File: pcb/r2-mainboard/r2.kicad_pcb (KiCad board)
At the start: 2 copper layers, 185.5 x 95 mm, 22 parts, among them J21 MICRO_SD(TFC-WPAPR-08), J22 HC-FPC-05-09-6RLTAG, J23 HC-FPC-05-09-6RLTAG, J24 HC-FPC-05-09-8RLTAG, J25 SolderPads 3x, J26 BTH-060-01-L-D-A-K-TR, J27 BTH-060-01-L-D-A-K-TR, J6 FPC-05F-50PH20, U13 TPS63802DLAR, U41 XC6SLX-FTG256, U52 MT41K64M16TW, U53 LM3630A, X2 PCM-071

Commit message: R2: a script to repair KiCad's library paths, instead of instructions
The owner does not run the AppImage -- KiCad is an extracted AppDir at
~/Apps/kicad-10.0.4 (a symlink to ./AppDir) launched via AppRun. That makes
the diagnosis better, not worse: /tmp/.mount_<random> is where an AppImage
mounts itself while running, so the entry in fp-lib-table is a leftover
written during an AppImage run before the extraction, and dead ever since.
The symbol table never broke because it was written with absolute paths.

tools/fix_kicad_paths.sh replaces the hand instructions. It derives the
paths from the install rather than hardcoding them, verifies all 155
library paths exist BEFORE installing anything, backs up both files with a
timestamp, and refuses to run while KiCad is open -- KiCad rewrites these
on exit and would silently undo the fix. It also sets the three path
variables, which were literally "vars": null, and then probes four
footprints and the 3D model tree to prove the result rather than assert it.

Dry-run against a copy of the real config: 155 libraries installed and
verified, the three variables set, every other key in kicad_common.json
preserved, and the real config untouched.

Co-Authored-By: Claude Opus 5 <noreply@anthropic.com>
Claude-Session: https://claude.ai/code/session_01MnesETWABbVdbcVnCKfKVs
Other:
- copper layers 2 -> 4
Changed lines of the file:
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@@
 	(generator_version "10.0")
 	(general
-		(thickness 1.6)
+		(thickness 1.0044)
 		(legacy_teardrops no)
 	)
@@
 	(layers
 		(0 "F.Cu" signal)
+		(4 "In1.Cu" power)
+		(6 "In2.Cu" mixed)
 		(2 "B.Cu" signal)
 		(9 "F.Adhes" user "F.Adhesive")
@@
 	)
 	(setup
+		(stackup
+			(layer "F.SilkS"
+				(type "Top Silk Screen")
+				(color "White")
+			)
+			(layer "F.Paste"
+				(type "Top Solder Paste")
+			)
+			(layer "F.Mask"
+				(type "Top Solder Mask")
+				(color "Green")
+				(thickness 0.025)
+			)
+			(layer "F.Cu"
+				(type "copper")
+				(thickness 0.035)
+			)
+			(layer "dielectric 1"
+				(type "prepreg")
+				(thickness 0.127)
+				(material "FR4")
+				(epsilon_r 4.2)
+				(loss_tangent 0.02)
+			)
+			(layer "In1.Cu"
+				(type "copper")
+				(thickness 0.0152)
+			)
+			(layer "dielectric 2"
+				(type "core")
+				(thickness 0.6)
+				(material "FR4")
+				(epsilon_r 4.2)
+				(loss_tangent 0.02)
+			)
+			(layer "In2.Cu"
+				(type "copper")
+				(thickness 0.0152)
+			)
+			(layer "dielectric 3"
+				(type "prepreg")
+				(thickness 0.127)
+				(material "FR4")
+				(epsilon_r 4.2)
+				(loss_tangent 0.02)
+			)
+			(layer "B.Cu"
+				(type "copper")
+				(thickness 0.035)
+			)
+			(layer "B.Mask"
+				(type "Bottom Solder Mask")
+				(color "Green")
+				(thickness 0.025)
+			)
+			(layer "B.Paste"
+				(type "Bottom Solder Paste")
+			)
+			(layer "B.SilkS"
+				(type "Bottom Silk Screen")
+				(color "White")
+			)
+			(copper_finish "ENIG")
+			(dielectric_constraints no)
+		)
 		(pad_to_mask_clearance 0)
 		(allow_soldermask_bridges_in_footprints no)
@@
 		(capping no)
 		(filling no)
+		(zone_defaults)
 		(pcbplotparams
 			(layerselection 0x00000000_00000000_55555555_5755f5ff)
@@
 		)
 		(embedded_fonts no)
-		(model "${KICAD8_3DMODEL_DIR}/Diode_SMD.3dshapes/D_SOD-323.wrl"
+		(model "${KICAD10_3DMODEL_DIR}/Diode_SMD.3dshapes/D_SOD-323.step"
 			(offset
 				(xyz 0 0 0)
@@
 		)
 		(embedded_fonts no)
-		(model "${KICAD6_3DMODEL_DIR}/Package_BGA.3dshapes/BGA-96_9.0x13.0mm_Layout2x3x16_P0.8mm.wrl"
+		(model "${KICAD10_3DMODEL_DIR}/Package_BGA.3dshapes/BGA-96_9.0x13.0mm_Layout2x3x16_P0.8mm.step"
 			(offset
 				(xyz 0 0 0)
@@
 		)
 		(embedded_fonts no)
-		(model "${KICAD8_3DMODEL_DIR}/Diode_SMD.3dshapes/D_SOD-323.wrl"
+		(model "${KICAD10_3DMODEL_DIR}/Diode_SMD.3dshapes/D_SOD-323.step"
 			(offset
 				(xyz 0 0 0)
@@
 		)
 		(embedded_fonts no)
-		(model "${KICAD8_3DMODEL_DIR}/Connector_FFC-FPC.3dshapes/Hirose_FH12-8S-0.5SH_1x08-1MP_P0.50mm_Horizontal.wrl"
+		(model "${KICAD10_3DMODEL_DIR}/Connector_FFC-FPC.3dshapes/Hirose_FH12-8S-0.5SH_1x08-1MP_P0.50mm_Horizontal.step"
 			(offset
 				(xyz 0 0 0)
@@
 		)
 		(embedded_fonts no)
-		(model "${KICAD8_3DMODEL_DIR}/Diode_SMD.3dshapes/D_SOD-323.wrl"
+		(model "${KICAD10_3DMODEL_DIR}/Diode_SMD.3dshapes/D_SOD-323.step"
 			(offset
 				(xyz 0 0 0)
@@
 		)
 		(embedded_fonts no)
-		(model "${KICAD8_3DMODEL_DIR}/Diode_SMD.3dshapes/D_SOD-323.wrl"
+		(model "${KICAD10_3DMODEL_DIR}/Diode_SMD.3dshapes/D_SOD-323.step"
 			(offset
 				(xyz 0 0 0)
@@
 		)
 		(embedded_fonts no)
-		(model "${KICAD8_3DMODEL_DIR}/Connector_FFC-FPC.3dshapes/Hirose_FH12-8S-0.5SH_1x08-1MP_P0.50mm_Horizontal.wrl"
+		(model "${KICAD10_3DMODEL_DIR}/Connector_FFC-FPC.3dshapes/Hirose_FH12-8S-0.5SH_1x08-1MP_P0.50mm_Horizontal.step"
 			(offset
 				(xyz 0 0 0)
@@
 		)
 		(embedded_fonts no)
-		(model "${KICAD8_3DMODEL_DIR}/Diode_SMD.3dshapes/D_SOD-323.wrl"
+		(model "${KICAD10_3DMODEL_DIR}/Diode_SMD.3dshapes/D_SOD-323.step"
 			(offset
 				(xyz 0 0 0)
@@
 		)
 		(embedded_fonts no)
-		(model "${KICAD8_3DMODEL_DIR}/Diode_SMD.3dshapes/D_SOD-323.wrl"
+		(model "${KICAD10_3DMODEL_DIR}/Diode_SMD.3dshapes/D_SOD-323.step"
 			(offset
 				(xyz 0 0 0)
@@
 		)
 		(embedded_fonts no)
-		(model "${KICAD8_3DMODEL_DIR}/Diode_SMD.3dshapes/D_SOD-323.wrl"
+		(model "${KICAD10_3DMODEL_DIR}/Diode_SMD.3dshapes/D_SOD-323.step"
 			(offset
 				(xyz 0 0 0)
@@
 		)
 		(embedded_fonts no)
-		(model "${KICAD8_3DMODEL_DIR}/Diode_SMD.3dshapes/D_SOD-323.wrl"
+		(model "${KICAD10_3DMODEL_DIR}/Diode_SMD.3dshapes/D_SOD-323.step"
 			(offset
 				(xyz 0 0 0)
@@
 		)
 		(embedded_fonts no)
-		(model "${KICAD8_3DMODEL_DIR}/Diode_SMD.3dshapes/D_SOD-323.wrl"
+		(model "${KICAD10_3DMODEL_DIR}/Diode_SMD.3dshapes/D_SOD-323.step"
 			(offset
 				(xyz 0 0 0)

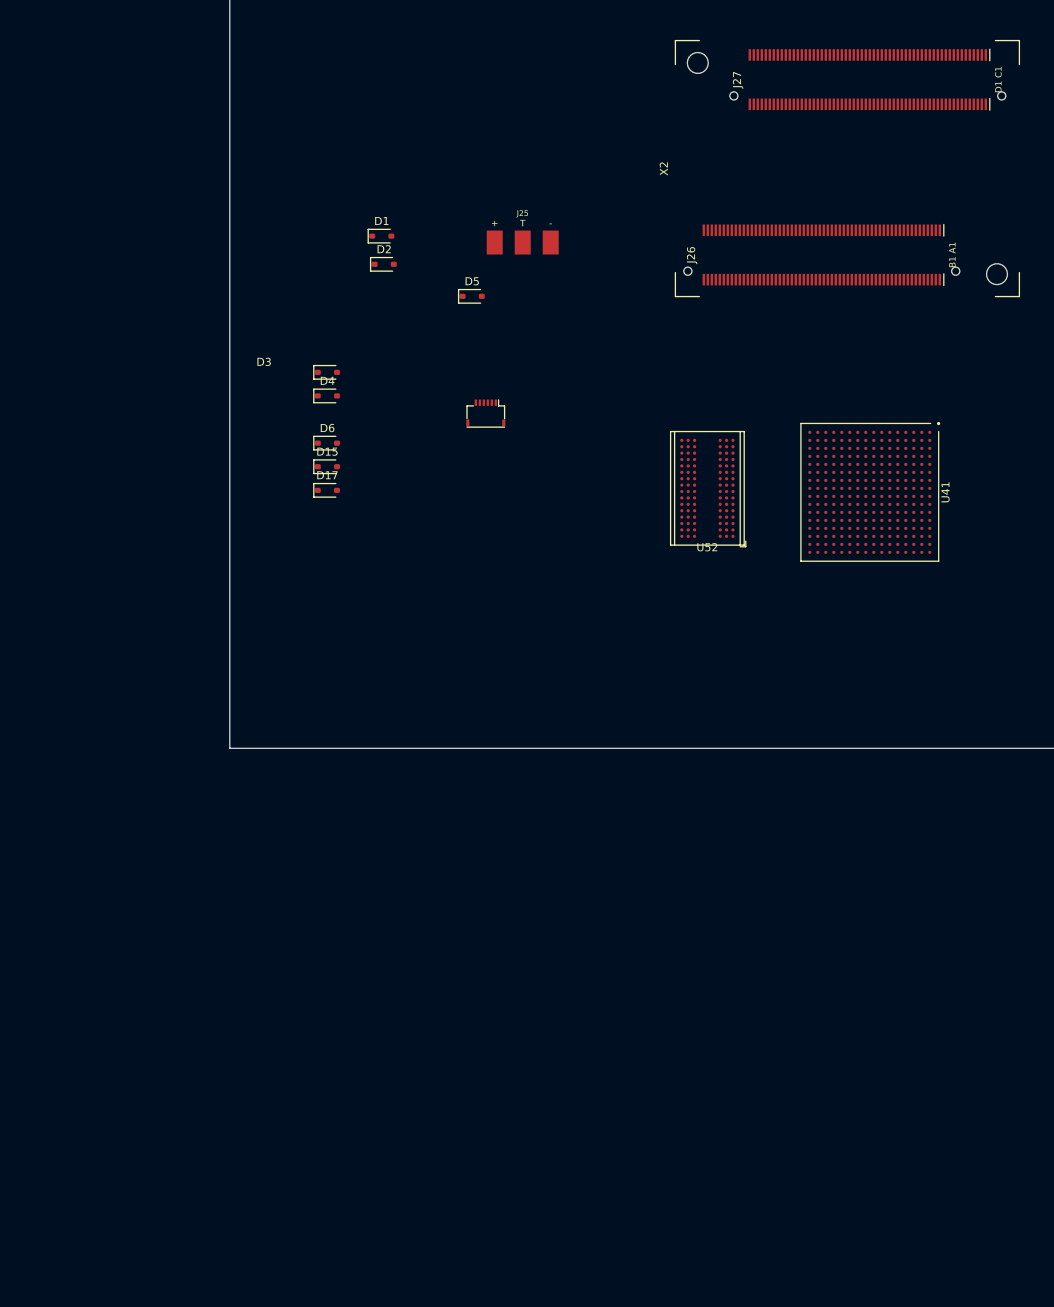
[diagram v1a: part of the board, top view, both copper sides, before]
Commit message: R2: place the two receptacles from X2, and fix three bugs found doing it
The connectors move as one now. tools/place_som.py reads X2's position and
rotation, snaps J26/J27 onto their exact offsets, and puts all three into a
KiCad group -- so from here you drag the SoM, not three parts that have to
agree with each other. It backs up the board, refuses to run while KiCad is
open, and re-runs the geometry check to prove its own result.

That symmetry is the reason this is a tool and not an instruction: the two
offsets are exact negatives about X2's origin, so an error of the wrong kind
does not shift a connector slightly, it puts J26 where J27 belongs. The
module still seats and every one of 240 nets is on the wrong receptacle.

Three bugs, all mine:

1. check_pcb_connectors.py had the rotation sign backwards, which SWAPPED
   the two expected positions. It reported a hand placement that was 0.9 mm
   and 0.2 mm out as 22 mm out, and would equally have blessed a board with
   the connectors exchanged. Settled empirically from a drill export rather
   than by reasoning: J26's alignment holes are asymmetric in x, so they
   distinguish the conventions. Confirmed twice, against X2's M2.5 holes too.

2. gen_som_footprint.py wrote (layer "User.Drawings"), which is KiCad's
   display alias; a board file needs the canonical Dwgs.User. The footprint
   editor accepts the alias, so the library exported fine -- but on import
   Pcbnew put those rects on a layer literally named "Rescue", and from then
   on kicad-cli could not read the board at all. Every pcb subcommand had
   been failing since the board was created.

3. Which made a third bug visible: check_pcb.py read /tmp/r2-drc.json
   without checking that the run succeeded, so it reported the previous
   run's numbers. A board that would not open was described as having 4250
   DRC violations. It now deletes the report first and says DID NOT RUN.

Real DRC, now that it runs: 742 violations, 499 unconnected -- which is what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
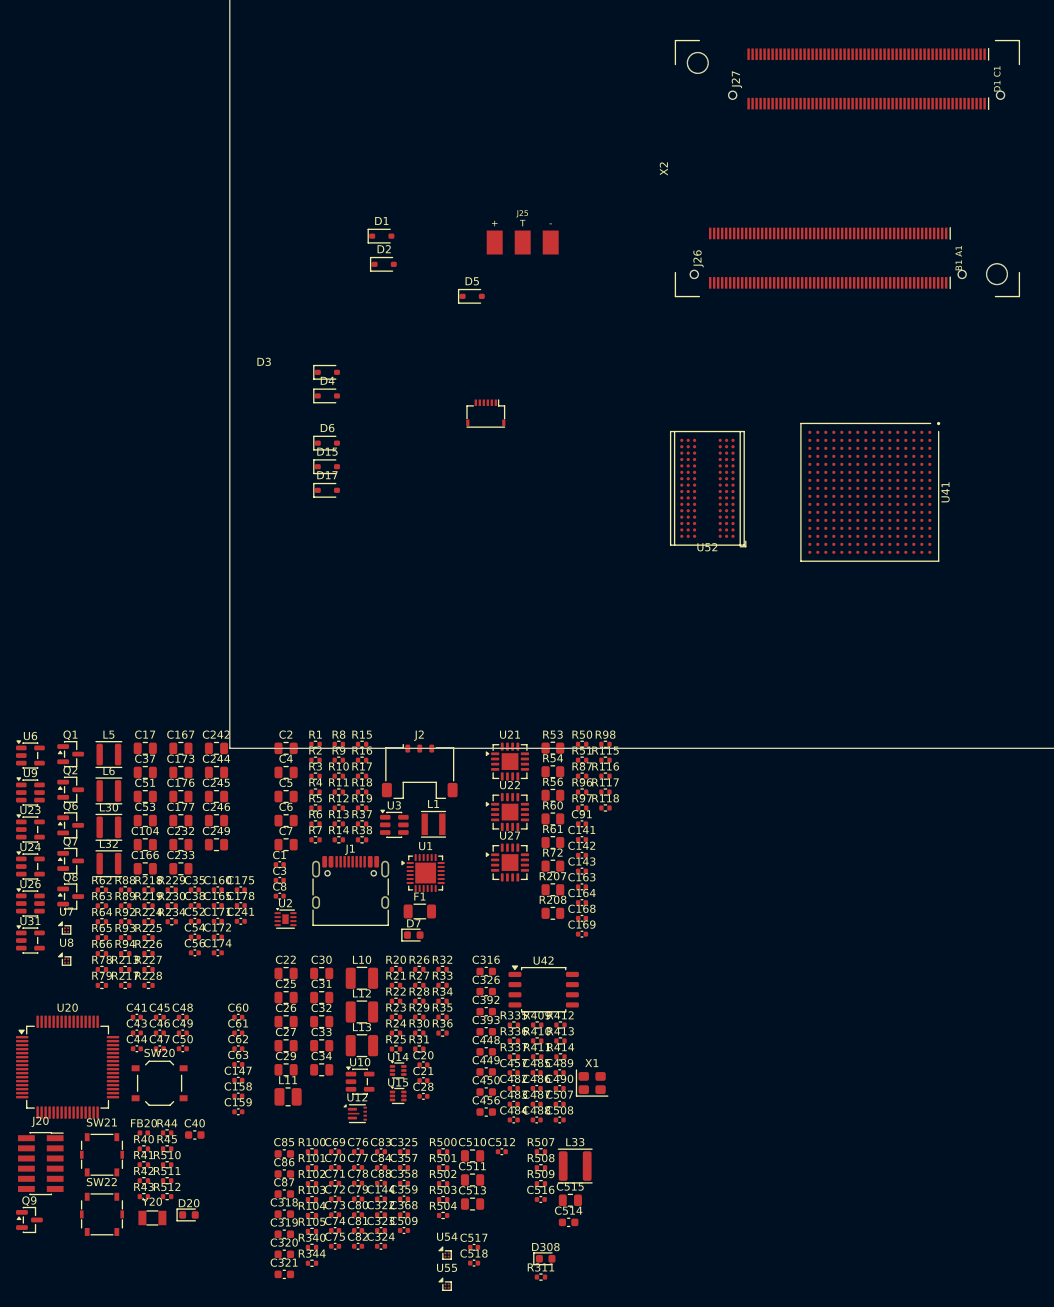
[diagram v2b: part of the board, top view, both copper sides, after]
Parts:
- added C1: 1uF/25V, Capacitor_SMD:C_0402_1005Metric, F.Cu at (93.2, 128.0)
- added C104: 22uF/10V, Capacitor_SMD:C_0805_2012Metric, F.Cu at (76.4, 125.5)
- added C141: 100nF/50V, Capacitor_SMD:C_0402_1005Metric, F.Cu at (131.0, 124.9)
- added C142: 100nF/50V, Capacitor_SMD:C_0402_1005Metric, F.Cu at (131.0, 126.9)
- added C143: 100nF/50V, Capacitor_SMD:C_0402_1005Metric, F.Cu at (131.0, 128.8)
- added C144: 100nF/50V, Capacitor_SMD:C_0402_1005Metric, F.Cu at (105.9, 169.8)
- added C147: 100nF/50V, Capacitor_SMD:C_0402_1005Metric, F.Cu at (88.1, 155.0)
- added C158: 100nF/50V, Capacitor_SMD:C_0402_1005Metric, F.Cu at (88.1, 157.0)
- added C159: 100nF/50V, Capacitor_SMD:C_0402_1005Metric, F.Cu at (88.1, 158.9)
- added C160: 100nF/50V, Capacitor_SMD:C_0402_1005Metric, F.Cu at (85.5, 131.2)
- added C163: 1nF/25V, Capacitor_SMD:C_0402_1005Metric, F.Cu at (131.0, 130.8)
- added C164: 1nF/25V, Capacitor_SMD:C_0402_1005Metric, F.Cu at (131.0, 132.8)
- added C165: 18pF/50V, Capacitor_SMD:C_0402_1005Metric, F.Cu at (85.5, 133.2)
- added C166: 4.7uF/50V, Capacitor_SMD:C_0805_2012Metric, F.Cu at (76.4, 128.6)
- added C167: 4.7uF/50V, Capacitor_SMD:C_0805_2012Metric, F.Cu at (80.9, 113.5)
- added C168: 1nF/25V, Capacitor_SMD:C_0402_1005Metric, F.Cu at (131.0, 134.8)
- added C169: 1nF/25V, Capacitor_SMD:C_0402_1005Metric, F.Cu at (131.0, 136.7)
- added C17: 22uF/10V, Capacitor_SMD:C_0805_2012Metric, F.Cu at (76.4, 113.5)
- added C171: 100nF/50V, Capacitor_SMD:C_0402_1005Metric, F.Cu at (85.5, 135.1)
- added C172: 470nF/25V, Capacitor_SMD:C_0402_1005Metric, F.Cu at (85.5, 137.1)
- added C173: 4.7uF/50V, Capacitor_SMD:C_0805_2012Metric, F.Cu at (80.9, 116.5)
- added C174: 100nF/50V, Capacitor_SMD:C_0402_1005Metric, F.Cu at (85.5, 139.1)
- added C175: 18pF/50V, Capacitor_SMD:C_0402_1005Metric, F.Cu at (88.4, 131.2)
- added C176: 4.7uF/50V, Capacitor_SMD:C_0805_2012Metric, F.Cu at (80.9, 119.5)
- added C177: 4.7uF/50V, Capacitor_SMD:C_0805_2012Metric, F.Cu at (80.9, 122.5)
- added C178: 470nF/25V, Capacitor_SMD:C_0402_1005Metric, F.Cu at (88.4, 133.2)
- added C2: 8.2uF/25V, Capacitor_SMD:C_0805_2012Metric, F.Cu at (94.0, 113.5)
- added C20: 1uF/16V, Capacitor_SMD:C_0402_1005Metric, F.Cu at (111.2, 153.1)
- added C21: 1uF/16V, Capacitor_SMD:C_0402_1005Metric, F.Cu at (111.2, 155.0)
- added C22: 22uF/10V, Capacitor_SMD:C_0805_2012Metric, F.Cu at (94.0, 141.6)
- added C232: 22uF/10V, Capacitor_SMD:C_0805_2012Metric, F.Cu at (80.9, 125.5)
- added C233: 4.7uF/50V, Capacitor_SMD:C_0805_2012Metric, F.Cu at (80.9, 128.6)
- added C241: 18pF/50V, Capacitor_SMD:C_0402_1005Metric, F.Cu at (88.4, 135.1)
- added C242: 22uF/10V, Capacitor_SMD:C_0805_2012Metric, F.Cu at (85.3, 113.5)
- added C244: 4.7uF/50V, Capacitor_SMD:C_0805_2012Metric, F.Cu at (85.3, 116.5)
- added C245: 22uF/10V, Capacitor_SMD:C_0805_2012Metric, F.Cu at (85.3, 119.5)
- added C246: 4.7uF/50V, Capacitor_SMD:C_0805_2012Metric, F.Cu at (85.3, 122.5)
- added C249: 22uF/10V, Capacitor_SMD:C_0805_2012Metric, F.Cu at (85.3, 125.5)
- added C25: 22uF/10V, Capacitor_SMD:C_0805_2012Metric, F.Cu at (94.0, 144.7)
- added C26: 22uF/10V, Capacitor_SMD:C_0805_2012Metric, F.Cu at (94.0, 147.7)
- added C27: 22uF/10V, Capacitor_SMD:C_0805_2012Metric, F.Cu at (94.0, 150.7)
- added C28: 100pF/50V, Capacitor_SMD:C_0402_1005Metric, F.Cu at (111.2, 157.0)
- added C29: 10uF/10V, Capacitor_SMD:C_0805_2012Metric, F.Cu at (94.0, 153.7)
- added C3: 47nF/25V, Capacitor_SMD:C_0402_1005Metric, F.Cu at (93.2, 130.0)
- added C30: 22uF/10V, Capacitor_SMD:C_0805_2012Metric, F.Cu at (98.5, 141.6)
- added C31: 4.7uF/10V, Capacitor_SMD:C_0805_2012Metric, F.Cu at (98.5, 144.7)
- added C316: 22uF/6.3V, Capacitor_SMD:C_0603_1608Metric, F.Cu at (119.1, 141.4)
- added C318: 22uF/6.3V, Capacitor_SMD:C_0603_1608Metric, F.Cu at (93.8, 171.7)
- added C319: 22uF/6.3V, Capacitor_SMD:C_0603_1608Metric, F.Cu at (93.8, 174.2)
- added C32: 22uF/10V, Capacitor_SMD:C_0805_2012Metric, F.Cu at (98.5, 147.7)
- added C320: 22uF/6.3V, Capacitor_SMD:C_0603_1608Metric, F.Cu at (93.8, 176.7)
- added C321: 22uF/6.3V, Capacitor_SMD:C_0603_1608Metric, F.Cu at (93.8, 179.3)
- added C322: 4.7uF/6.3V, Capacitor_SMD:C_0402_1005Metric, F.Cu at (105.9, 171.8)
- added C323: 4.7uF/6.3V, Capacitor_SMD:C_0402_1005Metric, F.Cu at (105.9, 173.8)
- added C324: 4.7uF/6.3V, Capacitor_SMD:C_0402_1005Metric, F.Cu at (105.9, 175.7)
- added C325: 470nF/25V, Capacitor_SMD:C_0402_1005Metric, F.Cu at (108.8, 163.9)
- added C326: 22uF/6.3V, Capacitor_SMD:C_0603_1608Metric, F.Cu at (119.1, 143.9)
- added C33: 4.7uF/10V, Capacitor_SMD:C_0805_2012Metric, F.Cu at (98.5, 150.7)
- added C34: 22uF/10V, Capacitor_SMD:C_0805_2012Metric, F.Cu at (98.5, 153.7)
- added C35: 100nF/50V, Capacitor_SMD:C_0402_1005Metric, F.Cu at (82.6, 131.2)
- added C357: 4.7uF/6.3V, Capacitor_SMD:C_0402_1005Metric, F.Cu at (108.8, 165.9)
- added C358: 470nF/25V, Capacitor_SMD:C_0402_1005Metric, F.Cu at (108.8, 167.9)
- added C359: 4.7uF/6.3V, Capacitor_SMD:C_0402_1005Metric, F.Cu at (108.8, 169.8)
- added C368: 470nF/25V, Capacitor_SMD:C_0402_1005Metric, F.Cu at (108.8, 171.8)
- added C37: 22uF/10V, Capacitor_SMD:C_0805_2012Metric, F.Cu at (76.4, 116.5)
- added C38: 18pF/50V, Capacitor_SMD:C_0402_1005Metric, F.Cu at (82.6, 133.2)
- added C392: 22uF/6.3V, Capacitor_SMD:C_0603_1608Metric, F.Cu at (119.1, 146.4)
- added C393: 22uF/6.3V, Capacitor_SMD:C_0603_1608Metric, F.Cu at (119.1, 148.9)
- added C4: 10uF/10V, Capacitor_SMD:C_0805_2012Metric, F.Cu at (94.0, 116.5)
- added C40: 4.7uF/10V, Capacitor_SMD:C_0603_1608Metric, F.Cu at (82.6, 161.8)
- added C41: 100nF/16V, Capacitor_SMD:C_0402_1005Metric, F.Cu at (75.4, 147.1)
- added C43: 1uF/16V, Capacitor_SMD:C_0402_1005Metric, F.Cu at (75.4, 149.1)
- added C44: 100nF/16V, Capacitor_SMD:C_0402_1005Metric, F.Cu at (75.4, 151.1)
- added C448: 22uF/6.3V, Capacitor_SMD:C_0603_1608Metric, F.Cu at (119.1, 151.4)
- added C449: 22uF/6.3V, Capacitor_SMD:C_0603_1608Metric, F.Cu at (119.1, 153.9)
- added C45: 100nF/16V, Capacitor_SMD:C_0402_1005Metric, F.Cu at (78.3, 147.1)
- added C450: 22uF/6.3V, Capacitor_SMD:C_0603_1608Metric, F.Cu at (119.1, 156.5)
- added C456: 22uF/6.3V, Capacitor_SMD:C_0603_1608Metric, F.Cu at (119.1, 159.0)
- added C457: 4.7uF/6.3V, Capacitor_SMD:C_0402_1005Metric, F.Cu at (122.5, 154.0)
- added C46: 18pF/50V, Capacitor_SMD:C_0402_1005Metric, F.Cu at (78.3, 149.1)
- added C47: 18pF/50V, Capacitor_SMD:C_0402_1005Metric, F.Cu at (78.3, 151.1)
- added C48: 100nF/16V, Capacitor_SMD:C_0402_1005Metric, F.Cu at (81.1, 147.1)
- added C482: 4.7uF/6.3V, Capacitor_SMD:C_0402_1005Metric, F.Cu at (122.5, 156.0)
- added C483: 4.7uF/6.3V, Capacitor_SMD:C_0402_1005Metric, F.Cu at (122.5, 158.0)
- added C484: 4.7uF/6.3V, Capacitor_SMD:C_0402_1005Metric, F.Cu at (122.5, 160.0)
- added C485: 470nF/25V, Capacitor_SMD:C_0402_1005Metric, F.Cu at (125.4, 154.0)
- added C486: 470nF/25V, Capacitor_SMD:C_0402_1005Metric, F.Cu at (125.4, 156.0)
- added C487: 470nF/25V, Capacitor_SMD:C_0402_1005Metric, F.Cu at (125.4, 158.0)
- added C488: 470nF/25V, Capacitor_SMD:C_0402_1005Metric, F.Cu at (125.4, 160.0)
- added C489: 470nF/25V, Capacitor_SMD:C_0402_1005Metric, F.Cu at (128.2, 154.0)
- added C49: 100nF/16V, Capacitor_SMD:C_0402_1005Metric, F.Cu at (81.1, 149.1)
- added C490: 470nF/25V, Capacitor_SMD:C_0402_1005Metric, F.Cu at (128.2, 156.0)
- added C5: 10uF/10V, Capacitor_SMD:C_0805_2012Metric, F.Cu at (94.0, 119.5)
- added C50: 100nF/16V, Capacitor_SMD:C_0402_1005Metric, F.Cu at (81.1, 151.1)
- added C507: 470nF/25V, Capacitor_SMD:C_0402_1005Metric, F.Cu at (128.2, 158.0)
- added C508: 100nF/16V, Capacitor_SMD:C_0402_1005Metric, F.Cu at (128.2, 160.0)
- added C509: 4.7uF/6.3V, Capacitor_SMD:C_0402_1005Metric, F.Cu at (108.8, 173.8)
- added C51: 22uF/10V, Capacitor_SMD:C_0805_2012Metric, F.Cu at (76.4, 119.5)
- added C510: 22u, Capacitor_SMD:C_0805_2012Metric, F.Cu at (117.3, 164.4)
- added C511: 22u, Capacitor_SMD:C_0805_2012Metric, F.Cu at (117.3, 167.5)
- added C512: 100n, Capacitor_SMD:C_0402_1005Metric, F.Cu at (121.0, 163.9)
- added C513: 10u, Capacitor_SMD:C_0805_2012Metric, F.Cu at (117.3, 170.5)
- added C514: 4.7uF/10V, Capacitor_SMD:C_0603_1608Metric, F.Cu at (129.4, 172.8)
- added C515: 2.2uF/50V, Capacitor_SMD:C_0805_2012Metric, F.Cu at (129.6, 170.0)
- added C516: 100nF/16V, Capacitor_SMD:C_0402_1005Metric, F.Cu at (125.9, 169.9)
- added C517: 1uF/16V, Capacitor_SMD:C_0402_1005Metric, F.Cu at (117.5, 175.9)
- added C518: 1uF/16V, Capacitor_SMD:C_0402_1005Metric, F.Cu at (117.5, 177.8)
- added C52: 470nF/25V, Capacitor_SMD:C_0402_1005Metric, F.Cu at (82.6, 135.1)
- added C53: 22uF/10V, Capacitor_SMD:C_0805_2012Metric, F.Cu at (76.4, 122.5)
- added C54: 100nF/50V, Capacitor_SMD:C_0402_1005Metric, F.Cu at (82.6, 137.1)
- added C56: 4.7uF/6.3V, Capacitor_SMD:C_0402_1005Metric, F.Cu at (82.6, 139.1)
- added C6: 4.7uF/10V, Capacitor_SMD:C_0805_2012Metric, F.Cu at (94.0, 122.5)
- added C60: 100nF/50V, Capacitor_SMD:C_0402_1005Metric, F.Cu at (88.1, 147.1)
- added C61: 100nF/50V, Capacitor_SMD:C_0402_1005Metric, F.Cu at (88.1, 149.1)
- added C62: 100nF/50V, Capacitor_SMD:C_0402_1005Metric, F.Cu at (88.1, 151.1)
- added C63: 100nF/50V, Capacitor_SMD:C_0402_1005Metric, F.Cu at (88.1, 153.0)
- added C69: 470nF/25V, Capacitor_SMD:C_0402_1005Metric, F.Cu at (100.2, 163.9)
- added C7: 10uF/10V, Capacitor_SMD:C_0805_2012Metric, F.Cu at (94.0, 125.5)
- added C70: 470nF/25V, Capacitor_SMD:C_0402_1005Metric, F.Cu at (100.2, 165.9)
- added C71: 100nF/50V, Capacitor_SMD:C_0402_1005Metric, F.Cu at (100.2, 167.9)
- added C72: 100nF/50V, Capacitor_SMD:C_0402_1005Metric, F.Cu at (100.2, 169.8)
- added C73: 470nF/25V, Capacitor_SMD:C_0402_1005Metric, F.Cu at (100.2, 171.8)
- added C74: 100nF/50V, Capacitor_SMD:C_0402_1005Metric, F.Cu at (100.2, 173.8)
- added C75: 100nF/50V, Capacitor_SMD:C_0402_1005Metric, F.Cu at (100.2, 175.7)
- added C76: 100nF/50V, Capacitor_SMD:C_0402_1005Metric, F.Cu at (103.0, 163.9)
- added C77: 100nF/50V, Capacitor_SMD:C_0402_1005Metric, F.Cu at (103.0, 165.9)
- added C78: 100nF/50V, Capacitor_SMD:C_0402_1005Metric, F.Cu at (103.0, 167.9)
- added C79: 470nF/25V, Capacitor_SMD:C_0402_1005Metric, F.Cu at (103.0, 169.8)
- added C8: 100nF/16V, Capacitor_SMD:C_0402_1005Metric, F.Cu at (93.2, 132.0)
- added C80: 470nF/25V, Capacitor_SMD:C_0402_1005Metric, F.Cu at (103.0, 171.8)
- added C81: 470nF/25V, Capacitor_SMD:C_0402_1005Metric, F.Cu at (103.0, 173.8)
- added C82: 470nF/25V, Capacitor_SMD:C_0402_1005Metric, F.Cu at (103.0, 175.7)
- added C83: 470nF/25V, Capacitor_SMD:C_0402_1005Metric, F.Cu at (105.9, 163.9)
- added C84: 470nF/25V, Capacitor_SMD:C_0402_1005Metric, F.Cu at (105.9, 165.9)
- added C85: 22uF/6.3V, Capacitor_SMD:C_0603_1608Metric, F.Cu at (93.8, 164.2)
- added C86: 22uF/6.3V, Capacitor_SMD:C_0603_1608Metric, F.Cu at (93.8, 166.7)
- added C87: 22uF/6.3V, Capacitor_SMD:C_0603_1608Metric, F.Cu at (93.8, 169.2)
- added C88: 100nF/50V, Capacitor_SMD:C_0402_1005Metric, F.Cu at (105.9, 167.9)
- added C91: 1nF/50V, Capacitor_SMD:C_0402_1005Metric, F.Cu at (131.0, 122.9)
- added D20: GREEN, LED_SMD:LED_0603_1608Metric, F.Cu at (81.9, 171.8)
- added D308: LED GREEN, LED_SMD:LED_0603_1608Metric, F.Cu at (126.5, 177.3)
- added D7: LED green, LED_SMD:LED_0603_1608Metric, F.Cu at (110.0, 136.8)
- added F1: 1.5A hold, Resistor_SMD:R_1206_3216Metric, F.Cu at (110.8, 133.9)
- added FB20: 120R@100M, Inductor_SMD:L_0402_1005Metric, F.Cu at (76.3, 161.6)
- added J1: USB-C 16P, Connector_USB:USB_C_Receptacle_HRO_TYPE-C-31-M-12, F.Cu at (102.1, 131.7)
- added J2: Pico-Lock 504050-0391, Connector_Molex:Molex_Pico-Lock_504050-0391_1x03-1MP_P1.50mm_Horizontal, F.Cu at (110.7, 116.3)
- added J20: SWD+JTAG (DNP), Connector_PinSocket_1.27mm:PinSocket_2x06_P1.27mm_Vertical_SMD, F.Cu at (63.4, 165.4)
- added L1: 1uH/3A, Inductor_SMD:L_Taiyo-Yuden_NR-30xx, F.Cu at (112.5, 123.0)
- added L10: 1uH/3.8A, Inductor_SMD:L_1210_3225Metric, F.Cu at (103.5, 142.2)
- added L11: 0.47uH/4.9A, Inductor_SMD:L_1008_2520Metric, F.Cu at (94.3, 157.1)
- added L12: 1uH/3.8A, Inductor_SMD:L_1210_3225Metric, F.Cu at (103.5, 146.5)
- added L13: 1uH/3.8A, Inductor_SMD:L_1210_3225Metric, F.Cu at (103.5, 150.7)
- added L30: WPN3012H4R7MT, Inductor_SMD:L_Changjiang_FNR3012S, F.Cu at (71.9, 123.4)
- added L32: WPN3012H4R7MT, Inductor_SMD:L_Changjiang_FNR3012S, F.Cu at (71.9, 127.9)
- added L33: 10uH 2.4A Isat, Inductor_SMD:L_Changjiang_FNR4030S, F.Cu at (130.2, 165.7)
- added L5: WPN3012H4R7MT, Inductor_SMD:L_Changjiang_FNR3012S, F.Cu at (71.9, 114.3)
- added L6: WPN3012H4R7MT, Inductor_SMD:L_Changjiang_FNR3012S, F.Cu at (71.9, 118.8)
- added Q1: AO3401A, Package_TO_SOT_SMD:SOT-23, F.Cu at (67.1, 114.2)
- added Q2: S8050, Package_TO_SOT_SMD:SOT-23, F.Cu at (67.1, 118.7)
- added Q6: AO3400A, Package_TO_SOT_SMD:SOT-23, F.Cu at (67.1, 123.1)
- added Q7: AO3401A, Package_TO_SOT_SMD:SOT-23, F.Cu at (67.1, 127.6)
- added Q8: AO3401A, Package_TO_SOT_SMD:SOT-23, F.Cu at (67.1, 132.0)
- added Q9: AO3400A, Package_TO_SOT_SMD:SOT-23, F.Cu at (62.0, 172.5)
- added R1: 5.1k, Resistor_SMD:R_0402_1005Metric, F.Cu at (97.7, 113.0)
- added R10: 30.1k/1%, Resistor_SMD:R_0402_1005Metric, F.Cu at (100.6, 117.0)
- added R100: 100R/1%, Resistor_SMD:R_0402_1005Metric, F.Cu at (97.3, 163.9)
- added R101: 5.1K/1%, Resistor_SMD:R_0402_1005Metric, F.Cu at (97.3, 165.9)
- added R102: 240R/1%, Resistor_SMD:R_0402_1005Metric, F.Cu at (97.3, 167.9)
- added R103: 5.1K/1%, Resistor_SMD:R_0402_1005Metric, F.Cu at (97.3, 169.9)
- added R104: 1K/1%, Resistor_SMD:R_0402_1005Metric, F.Cu at (97.3, 171.9)
- added R105: 1K/1%, Resistor_SMD:R_0402_1005Metric, F.Cu at (97.3, 173.9)
- added R11: 0R, Resistor_SMD:R_0402_1005Metric, F.Cu at (100.6, 119.0)
- added R115: 1M/1%, Resistor_SMD:R_0402_1005Metric, F.Cu at (134.0, 115.0)
- added R116: 100K/1%, Resistor_SMD:R_0402_1005Metric, F.Cu at (134.0, 117.0)
- added R117: 1M/1%, Resistor_SMD:R_0402_1005Metric, F.Cu at (134.0, 119.0)
- added R118: 100K/1%, Resistor_SMD:R_0402_1005Metric, F.Cu at (134.0, 121.0)
- added R12: 100k/1%, Resistor_SMD:R_0402_1005Metric, F.Cu at (100.6, 121.0)
- added R13: 100k/1%, Resistor_SMD:R_0402_1005Metric, F.Cu at (100.6, 122.9)
- added R14: 0R, Resistor_SMD:R_0402_1005Metric, F.Cu at (100.6, 124.9)
- added R15: 0R, Resistor_SMD:R_0402_1005Metric, F.Cu at (103.5, 113.0)
- added R16: 10k, Resistor_SMD:R_0402_1005Metric, F.Cu at (103.5, 115.0)
- added R17: 100k, Resistor_SMD:R_0402_1005Metric, F.Cu at (103.5, 117.0)
- added R18: 100k, Resistor_SMD:R_0402_1005Metric, F.Cu at (103.5, 119.0)
- added R19: 10k, Resistor_SMD:R_0402_1005Metric, F.Cu at (103.5, 121.0)
- added R2: 5.1k, Resistor_SMD:R_0402_1005Metric, F.Cu at (97.7, 115.0)
- added R20: 100k, Resistor_SMD:R_0402_1005Metric, F.Cu at (107.8, 141.1)
- added R207: 20mR, Resistor_SMD:R_0805_2012Metric, F.Cu at (127.4, 131.2)
- added R208: 20mR, Resistor_SMD:R_0805_2012Metric, F.Cu at (127.4, 134.1)
- added R21: 732k/1%, Resistor_SMD:R_0402_1005Metric, F.Cu at (107.8, 143.1)
- added R213: 100K/1%, Resistor_SMD:R_0402_1005Metric, F.Cu at (73.9, 141.1)
- added R217: 10K/1%, Resistor_SMD:R_0402_1005Metric, F.Cu at (73.9, 143.1)
- added R218: 240K/1%, Resistor_SMD:R_0402_1005Metric, F.Cu at (76.8, 131.2)
- added R219: 10K/1%, Resistor_SMD:R_0402_1005Metric, F.Cu at (76.8, 133.2)
- added R22: 100k/1%, Resistor_SMD:R_0402_1005Metric, F.Cu at (107.8, 145.1)
- added R224: 390K/1%, Resistor_SMD:R_0402_1005Metric, F.Cu at (76.8, 135.2)
- added R225: 20.5K/1%, Resistor_SMD:R_0402_1005Metric, F.Cu at (76.8, 137.2)
- added R226: 100K/1%, Resistor_SMD:R_0402_1005Metric, F.Cu at (76.8, 139.2)
- added R227: 22K/1%, Resistor_SMD:R_0402_1005Metric, F.Cu at (76.8, 141.1)
- added R228: 100K/1%, Resistor_SMD:R_0402_1005Metric, F.Cu at (76.8, 143.1)
- added R229: 5.1K/1%, Resistor_SMD:R_0402_1005Metric, F.Cu at (79.7, 131.2)
- added R23: 0R, Resistor_SMD:R_0402_1005Metric, F.Cu at (107.8, 147.1)
- added R230: 5.1K/1%, Resistor_SMD:R_0402_1005Metric, F.Cu at (79.7, 133.2)
- added R234: 100K/1%, Resistor_SMD:R_0402_1005Metric, F.Cu at (79.7, 135.2)
- added R24: 511k/1%, Resistor_SMD:R_0402_1005Metric, F.Cu at (107.8, 149.1)
- added R25: 91k/1%, Resistor_SMD:R_0402_1005Metric, F.Cu at (107.8, 151.1)
- added R26: 100k, Resistor_SMD:R_0402_1005Metric, F.Cu at (110.7, 141.1)
- added R27: 0R, Resistor_SMD:R_0402_1005Metric, F.Cu at (110.7, 143.1)
- added R28: 470k, Resistor_SMD:R_0402_1005Metric, F.Cu at (110.7, 145.1)
- added R29: 100k/1%, Resistor_SMD:R_0402_1005Metric, F.Cu at (110.7, 147.1)
- added R3: 10k, Resistor_SMD:R_0402_1005Metric, F.Cu at (97.7, 117.0)
- added R30: 100k/1%, Resistor_SMD:R_0402_1005Metric, F.Cu at (110.7, 149.1)
- added R31: 100k, Resistor_SMD:R_0402_1005Metric, F.Cu at (110.7, 151.1)
- added R311: 10K/1%, Resistor_SMD:R_0402_1005Metric, F.Cu at (125.9, 179.6)
- added R32: 470k, Resistor_SMD:R_0402_1005Metric, F.Cu at (113.6, 141.1)
- added R33: 150k/1%, Resistor_SMD:R_0402_1005Metric, F.Cu at (113.6, 143.1)
- added R335: 5.1K/1%, Resistor_SMD:R_0402_1005Metric, F.Cu at (122.5, 148.1)
- added R336: 5.1K/1%, Resistor_SMD:R_0402_1005Metric, F.Cu at (122.5, 150.1)
- added R337: 1K/1%, Resistor_SMD:R_0402_1005Metric, F.Cu at (122.5, 152.1)
- added R34: 100k/1%, Resistor_SMD:R_0402_1005Metric, F.Cu at (113.6, 145.1)
- added R340: 100R/1%, Resistor_SMD:R_0402_1005Metric, F.Cu at (97.3, 175.9)
- added R344: 5.1K/1%, Resistor_SMD:R_0402_1005Metric, F.Cu at (97.3, 177.9)
- added R35: 100k, Resistor_SMD:R_0402_1005Metric, F.Cu at (113.6, 147.1)
- added R36: 470k, Resistor_SMD:R_0402_1005Metric, F.Cu at (113.6, 149.1)
- added R37: 1k, Resistor_SMD:R_0402_1005Metric, F.Cu at (103.5, 122.9)
- added R38: 10k, Resistor_SMD:R_0402_1005Metric, F.Cu at (103.5, 124.9)
- added R4: 10k, Resistor_SMD:R_0402_1005Metric, F.Cu at (97.7, 119.0)
- added R40: 10k, Resistor_SMD:R_0402_1005Metric, F.Cu at (76.3, 163.6)
- added R409: 33R/1%, Resistor_SMD:R_0402_1005Metric, F.Cu at (125.4, 148.1)
- added R41: 1k, Resistor_SMD:R_0402_1005Metric, F.Cu at (76.3, 165.6)
- added R410: 10k, Resistor_SMD:R_0402_1005Metric, F.Cu at (125.4, 150.1)
- added R411: 100R, Resistor_SMD:R_0402_1005Metric, F.Cu at (125.4, 152.1)
- added R412: 10k, Resistor_SMD:R_0402_1005Metric, F.Cu at (128.3, 148.1)
- added R413: 10k, Resistor_SMD:R_0402_1005Metric, F.Cu at (128.3, 150.1)
- added R414: 4.7k, Resistor_SMD:R_0402_1005Metric, F.Cu at (128.3, 152.1)
- added R42: 100k, Resistor_SMD:R_0402_1005Metric, F.Cu at (76.3, 167.5)
- added R43: 100k, Resistor_SMD:R_0402_1005Metric, F.Cu at (76.3, 169.5)
- added R44: 1k, Resistor_SMD:R_0402_1005Metric, F.Cu at (79.2, 161.6)
- added R45: 1k, Resistor_SMD:R_0402_1005Metric, F.Cu at (79.2, 163.6)
- added R5: 10k, Resistor_SMD:R_0402_1005Metric, F.Cu at (97.7, 121.0)
- added R50: 1M/1%, Resistor_SMD:R_0402_1005Metric, F.Cu at (131.0, 113.0)
- added R500: 47k, Resistor_SMD:R_0402_1005Metric, F.Cu at (113.7, 163.9)
- added R501: 47k, Resistor_SMD:R_0402_1005Metric, F.Cu at (113.7, 165.9)
- added R502: 47k, Resistor_SMD:R_0402_1005Metric, F.Cu at (113.7, 167.9)
- added R503: 47k, Resistor_SMD:R_0402_1005Metric, F.Cu at (113.7, 169.9)
- added R504: 47k, Resistor_SMD:R_0402_1005Metric, F.Cu at (113.7, 171.9)
- added R507: 100k, Resistor_SMD:R_0402_1005Metric, F.Cu at (125.9, 163.9)
- added R508: 10k, Resistor_SMD:R_0402_1005Metric, F.Cu at (125.9, 165.9)
- added R509: 0R, Resistor_SMD:R_0402_1005Metric, F.Cu at (125.9, 167.9)
- added R51: 100K/1%, Resistor_SMD:R_0402_1005Metric, F.Cu at (131.0, 115.0)
- added R510: 100k, Resistor_SMD:R_0402_1005Metric, F.Cu at (79.2, 165.6)
- added R511: 1k, Resistor_SMD:R_0402_1005Metric, F.Cu at (79.2, 167.5)
- added R512: 1M, Resistor_SMD:R_0402_1005Metric, F.Cu at (79.2, 169.5)
- added R53: 20mR, Resistor_SMD:R_0805_2012Metric, F.Cu at (127.4, 113.5)
- added R54: 20mR, Resistor_SMD:R_0805_2012Metric, F.Cu at (127.4, 116.4)
- added R56: 20mR, Resistor_SMD:R_0805_2012Metric, F.Cu at (127.4, 119.4)
- added R6: 2.2k, Resistor_SMD:R_0402_1005Metric, F.Cu at (97.7, 122.9)
- added R60: 20mR, Resistor_SMD:R_0805_2012Metric, F.Cu at (127.4, 122.3)
- added R61: 20mR, Resistor_SMD:R_0805_2012Metric, F.Cu at (127.4, 125.3)
- added R62: 100K/1%, Resistor_SMD:R_0402_1005Metric, F.Cu at (71.0, 131.2)
- added R63: 33R/1%, Resistor_SMD:R_0402_1005Metric, F.Cu at (71.0, 133.2)
- added R64: 22K/1%, Resistor_SMD:R_0402_1005Metric, F.Cu at (71.0, 135.2)
- added R65: 10K/1%, Resistor_SMD:R_0402_1005Metric, F.Cu at (71.0, 137.2)
- added R66: 33R/1%, Resistor_SMD:R_0402_1005Metric, F.Cu at (71.0, 139.2)
- added R7: 2.2k, Resistor_SMD:R_0402_1005Metric, F.Cu at (97.7, 124.9)
- added R72: 20mR, Resistor_SMD:R_0805_2012Metric, F.Cu at (127.4, 128.2)
- added R78: 150K/1%, Resistor_SMD:R_0402_1005Metric, F.Cu at (71.0, 141.1)
- added R79: 13K/1%, Resistor_SMD:R_0402_1005Metric, F.Cu at (71.0, 143.1)
- added R8: 260R/1%, Resistor_SMD:R_0402_1005Metric, F.Cu at (100.6, 113.0)
- added R87: 100K/1%, Resistor_SMD:R_0402_1005Metric, F.Cu at (131.0, 117.0)
- added R88: 390K/1%, Resistor_SMD:R_0402_1005Metric, F.Cu at (73.9, 131.2)
- added R89: 22K/1%, Resistor_SMD:R_0402_1005Metric, F.Cu at (73.9, 133.2)
- added R9: 5.23k/1%, Resistor_SMD:R_0402_1005Metric, F.Cu at (100.6, 115.0)
- added R92: 100K/1%, Resistor_SMD:R_0402_1005Metric, F.Cu at (73.9, 135.2)
- added R93: 100K/1%, Resistor_SMD:R_0402_1005Metric, F.Cu at (73.9, 137.2)
- added R94: 100K/1%, Resistor_SMD:R_0402_1005Metric, F.Cu at (73.9, 139.2)
- added R96: 1M/1%, Resistor_SMD:R_0402_1005Metric, F.Cu at (131.0, 119.0)
- added R97: 100K/1%, Resistor_SMD:R_0402_1005Metric, F.Cu at (131.0, 121.0)
- added R98: 1M/1%, Resistor_SMD:R_0402_1005Metric, F.Cu at (134.0, 113.0)
- added SW20: SW, Button_Switch_SMD:SW_Push_1P1T_XKB_TS-1187A, F.Cu at (78.2, 155.4)
- added SW21: SW, Button_Switch_SMD:SW_SPST_Panasonic_EVQPL_3PL_5PL_PT_A15, F.Cu at (71.0, 164.3)
- added SW22: SW, Button_Switch_SMD:SW_SPST_Panasonic_EVQPL_3PL_5PL_PT_A15, F.Cu at (71.0, 171.8)
- added U1: BQ25892RTW, Package_DFN_QFN:WQFN-24-1EP_4x4mm_P0.5mm_EP2.6x2.6mm, F.Cu at (111.5, 129.1)
- added U10: TPS7A0233DBVR, Package_TO_SOT_SMD:SOT-23-5, F.Cu at (103.3, 155.2)
- added U12: TPS61022RWUR, Package_DFN_QFN:Texas_RWU0007A_VQFN-7_2x2mm_P0.5mm, F.Cu at (103.0, 159.2)
- added U14: TPS62A02DRLR, Package_TO_SOT_SMD:SOT-563, F.Cu at (108.0, 153.8)
- added U15: TPS62A02DRLR, Package_TO_SOT_SMD:SOT-563, F.Cu at (108.0, 157.0)
- added U2: MAX17048G+T10, Package_DFN_QFN:TDFN-8-1EP_2x2mm_P0.5mm_EP0.8x1.2mm, F.Cu at (94.0, 134.8)
- added U20: STM32G0B1RCT6, Package_QFP:LQFP-64_10x10mm_P0.5mm, F.Cu at (66.7, 153.4)
- added U21: INA3221, Package_DFN_QFN:Texas_RGV0016A_VQFN-16-1EP_4x4mm_P0.65mm_EP2.1x2.1mm, F.Cu at (122.0, 115.2)
- added U22: INA3221, Package_DFN_QFN:Texas_RGV0016A_VQFN-16-1EP_4x4mm_P0.65mm_EP2.1x2.1mm, F.Cu at (122.0, 121.5)
- added U23: LGS6302B5, Package_TO_SOT_SMD:SOT-23-5, F.Cu at (62.1, 123.7)
- added U24: LGS6302B5, Package_TO_SOT_SMD:SOT-23-5, F.Cu at (62.1, 128.3)
- added U26: LGS5145, Package_TO_SOT_SMD:TSOT-23-6, F.Cu at (62.1, 132.9)
- added U27: INA3221, Package_DFN_QFN:Texas_RGV0016A_VQFN-16-1EP_4x4mm_P0.65mm_EP2.1x2.1mm, F.Cu at (122.0, 127.8)
- added U3: USBLC6-2SC6, Package_TO_SOT_SMD:SOT-23-6, F.Cu at (107.6, 123.1)
- added U31: LM321, Package_TO_SOT_SMD:SOT-23-5, F.Cu at (62.1, 137.5)
- added U42: W25Q128JVSIQ, Package_SO:SOIC-8_5.3x5.3mm_P1.27mm, F.Cu at (126.2, 143.7)
- added U54: TPS22914BYFPR, Package_BGA:WLP-4_0.83x0.83mm_P0.4mm, F.Cu at (114.2, 176.8)
- added U55: TPS22914BYFPR, Package_BGA:WLP-4_0.83x0.83mm_P0.4mm, F.Cu at (114.2, 180.7)
- added U6: MT9700, Package_TO_SOT_SMD:SOT-23-5, F.Cu at (62.1, 114.4)
- added U7: TPS22914BYFPR, Package_BGA:WLP-4_0.83x0.83mm_P0.4mm, F.Cu at (66.6, 136.2)
- added U8: TPS22914BYFPR, Package_BGA:WLP-4_0.83x0.83mm_P0.4mm, F.Cu at (66.6, 140.1)
- added U9: LGS5145, Package_TO_SOT_SMD:TSOT-23-6, F.Cu at (62.1, 119.0)
- added X1: 33.33MHz, Oscillator:Oscillator_SMD_Abracon_ASE-4Pin_3.2x2.5mm, F.Cu at (132.3, 155.3)
- added Y20: 32.768kHz, Crystal:Crystal_SMD_3215-2Pin_3.2x1.5mm, F.Cu at (77.3, 172.2)
- moved J26 0.89 mm to (161.8, 52.2)
- moved J27 0.17 mm to (166.6, 29.8)
